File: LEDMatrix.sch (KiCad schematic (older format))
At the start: 75 parts, among them SW1 SW_Push_LED, SW10 SW_Push_LED, SW11 SW_Push_LED, SW12 SW_Push_LED, SW13 SW_Push_LED, SW14 SW_Push_LED, SW15 SW_Push_LED, SW16 SW_Push_LED, SW17 SW_Push_LED, SW18 SW_Push_LED, SW19 SW_Push_LED, SW2 SW_Push_LED, SW20 SW_Push_LED, SW21 SW_Push_LED, SW22 SW_Push_LED, SW23 SW_Push_LED, SW24 SW_Push_LED, SW25 SW_Push_LED, SW26 SW_Push_LED, SW27 SW_Push_LED, SW28 SW_Push_LED, SW29 SW_Push_LED, SW3 SW_Push_LED, SW30 SW_Push_LED, SW31 SW_Push_LED, SW32 SW_Push_LED, SW33 SW_Push_LED, SW34 SW_Push_LED, SW35 SW_Push_LED, SW36 SW_Push_LED, SW37 SW_Push_LED, SW38 SW_Push_LED, SW39 SW_Push_LED, SW4 SW_Push_LED, SW40 SW_Push_LED, SW41 SW_Push_LED, SW42 SW_Push_LED, SW43 SW_Push_LED, SW44 SW_Push_LED, SW45 SW_Push_LED, SW46 SW_Push_LED, SW47 SW_Push_LED, SW48 SW_Push_LED, SW49 SW_Push_LED, SW5 SW_Push_LED, SW50 SW_Push_LED, SW51 SW_Push_LED, SW52 SW_Push_LED, SW53 SW_Push_LED, SW54 SW_Push_LED, SW55 SW_Push_LED, SW56 SW_Push_LED, SW57 SW_Push_LED, SW58 SW_Push_LED, SW59 SW_Push_LED, SW6 SW_Push_LED, SW60 SW_Push_LED, SW61 SW_Push_LED, SW62 SW_Push_LED, SW63 SW_Push_LED, SW64 SW_Push_LED, SW7 SW_Push_LED, SW8 SW_Push_LED, SW9 SW_Push_LED

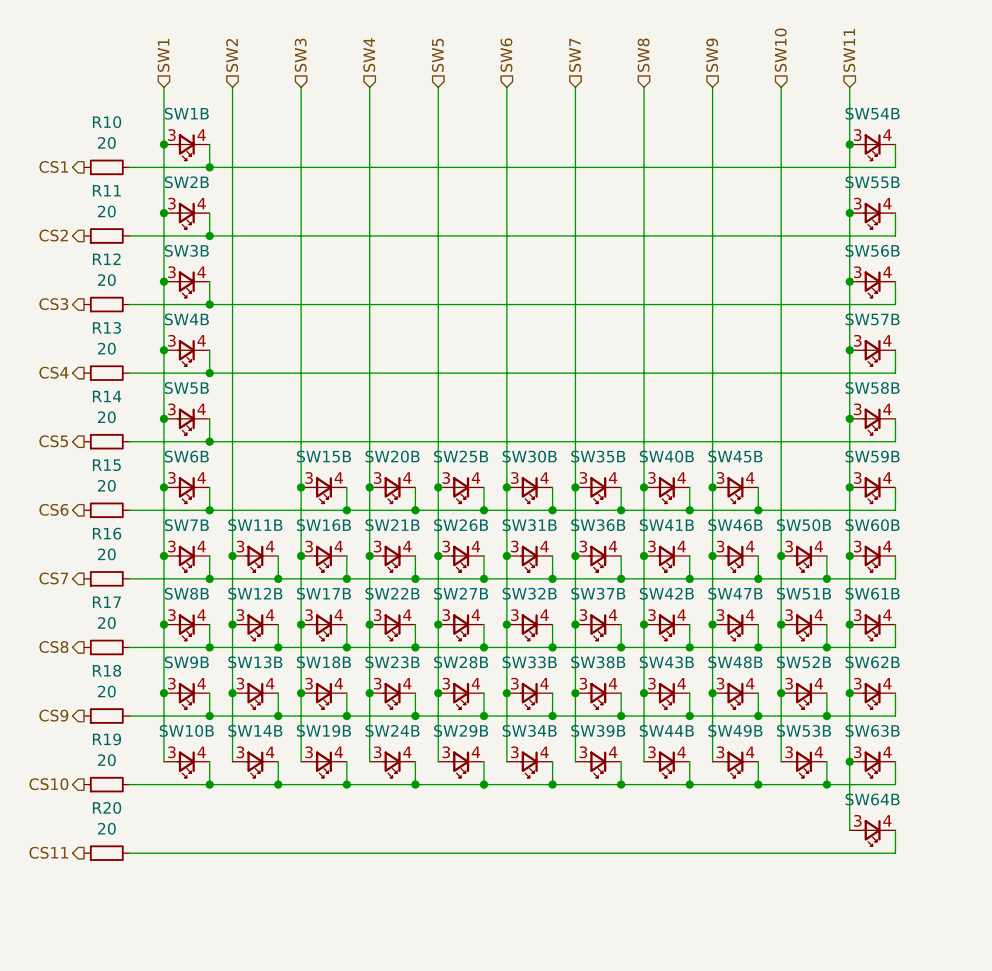
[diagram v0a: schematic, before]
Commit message: Add ATmega32u4 to board
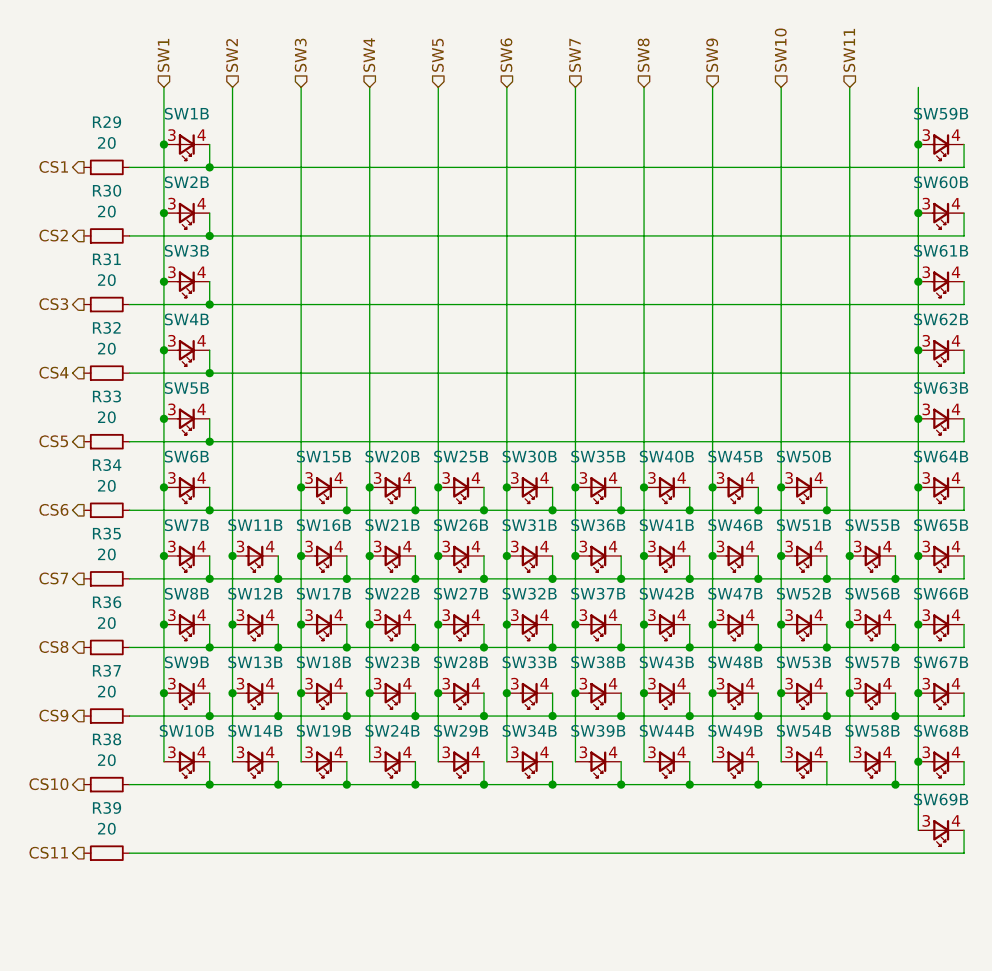
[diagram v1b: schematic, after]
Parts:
- added SW50, SW55, SW56, SW57, SW58: SW_Push_LED, Collins-FMS-3000:SW_PUSH_6mm, symbol Collins-FMS-3000:SW_Push_LED
- R29: renamed from R10; footprint (none) -> Resistor_SMD:R_0402_1005Metric
- R30: renamed from R11; footprint (none) -> Resistor_SMD:R_0402_1005Metric
- R31: renamed from R12; footprint (none) -> Resistor_SMD:R_0402_1005Metric
- R32: renamed from R13; footprint (none) -> Resistor_SMD:R_0402_1005Metric
- R33: renamed from R14; footprint (none) -> Resistor_SMD:R_0402_1005Metric
- R34: renamed from R15; footprint (none) -> Resistor_SMD:R_0402_1005Metric
- R35: renamed from R16; footprint (none) -> Resistor_SMD:R_0402_1005Metric
- R36: renamed from R17; footprint (none) -> Resistor_SMD:R_0402_1005Metric
- R37: renamed from R18; footprint (none) -> Resistor_SMD:R_0402_1005Metric
- R38: renamed from R19; footprint (none) -> Resistor_SMD:R_0402_1005Metric
- R39: renamed from R20; footprint (none) -> Resistor_SMD:R_0402_1005Metric
- SW1, SW10, SW11, SW12, SW13, SW14, SW15, SW16, SW17, SW18, SW19, SW2, SW20, SW21, SW22, SW23, SW24, SW25, SW26, SW27, SW28, SW29, SW3, SW30, SW31, SW32, SW33, SW34, SW35, SW36, SW37, SW38, SW39, SW4, SW40, SW41, SW42, SW43, SW44, SW45, SW46, SW47, SW48, SW49, SW5, SW6, SW7, SW8, SW9: footprint (none) -> Collins-FMS-3000:SW_PUSH_6mm
- SW51: renamed from SW50; footprint (none) -> Collins-FMS-3000:SW_PUSH_6mm
- SW52: renamed from SW51; footprint (none) -> Collins-FMS-3000:SW_PUSH_6mm
- SW53: renamed from SW52; footprint (none) -> Collins-FMS-3000:SW_PUSH_6mm
- SW54: renamed from SW53; footprint (none) -> Collins-FMS-3000:SW_PUSH_6mm
- SW59: renamed from SW54; footprint (none) -> Collins-FMS-3000:SW_PUSH_6mm
- SW60: renamed from SW55; footprint (none) -> Collins-FMS-3000:SW_PUSH_6mm
- SW61: renamed from SW56; footprint (none) -> Collins-FMS-3000:SW_PUSH_6mm
- SW62: renamed from SW57; footprint (none) -> Collins-FMS-3000:SW_PUSH_6mm
- SW63: renamed from SW58; footprint (none) -> Collins-FMS-3000:SW_PUSH_6mm
- SW64: renamed from SW59; footprint (none) -> Collins-FMS-3000:SW_PUSH_6mm
- SW65: renamed from SW60; footprint (none) -> Collins-FMS-3000:SW_PUSH_6mm
- SW66: renamed from SW61; footprint (none) -> Collins-FMS-3000:SW_PUSH_6mm
- SW67: renamed from SW62; footprint (none) -> Collins-FMS-3000:SW_PUSH_6mm
- SW68: renamed from SW63; footprint (none) -> Collins-FMS-3000:SW_PUSH_6mm
- SW69: renamed from SW64; footprint (none) -> Collins-FMS-3000:SW_PUSH_6mm
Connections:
- net SW10: now also SW50.3
- net SW11: now also SW55.3, SW56.3, SW57.3, SW58.3; no longer SW59.3, SW60.3, SW61.3, SW62.3, SW63.3, SW64.3, SW65.3, SW66.3, SW67.3, SW68.3, SW69.3
- net at R34.2, SW15.4, SW20.4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: now also SW50.4
- net at R35.2, SW11.4, SW16.4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: now also SW55.4
- net at R36.2, SW12.4, SW17.4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: now also SW56.4
- net at R37.2, SW13.4, SW18.4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: now also SW57.4
- net at R38.2, SW10.4, SW14.4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: now also SW58.4
- new net: SW59.3, SW60.3, SW61.3, SW62.3, SW63.3, SW64.3, SW65.3, SW66.3, SW67.3, SW68.3, SW69.3
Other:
- moved on the sheet: SW59B, SW60B, SW61B, SW62B, SW63B, SW64B, SW65B, SW66B, SW67B, SW68B, SW69B

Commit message: Redo the LED matrix
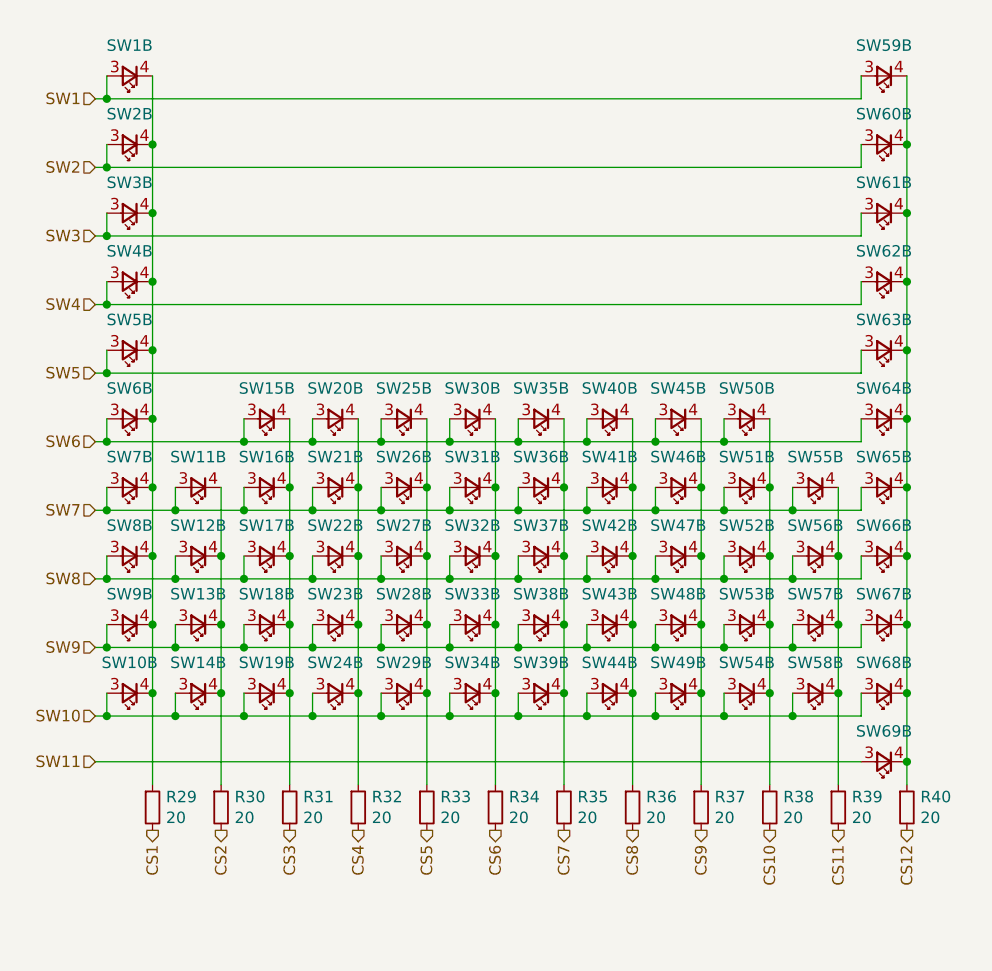
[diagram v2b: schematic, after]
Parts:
- added R40: 20, symbol Device:R_Small
- R29, R30, R31, R32, R33, R34, R35, R36, R37, R38, R39: footprint Resistor_SMD:R_0402_1005Metric -> (none)
- SW1, SW10, SW11, SW12, SW13, SW14, SW15, SW16, SW17, SW18, SW19, SW2, SW20, SW21, SW22, SW23, SW24, SW25, SW26, SW27, SW28, SW29, SW3, SW30, SW31, SW32, SW33, SW34, SW35, SW36, SW37, SW38, SW39, SW4, SW40, SW41, SW42, SW43, SW44, SW45, SW46, SW47, SW48, SW49, SW5, SW50, SW51, SW52, SW53, SW54, SW55, SW56, SW57, SW58, SW59, SW6, SW60, SW61, SW62, SW63, SW64, SW65, SW66, SW67, SW68, SW69, SW7, SW8, SW9: footprint Collins-FMS-3000:SW_PUSH_6mm -> (none)
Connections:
- net CS1: now also R29.2; no longer R29.1
- net CS10: now also R38.2; no longer R38.1
- net CS11: now also R39.2; no longer R39.1
- net CS2: now also R30.2; no longer R30.1
- net CS3: now also R31.2; no longer R31.1
- net CS4: now also R32.2; no longer R32.1
- net CS5: now also R33.2; no longer R33.1
- net CS6: now also R34.2; no longer R34.1
- net CS7: now also R35.2; no longer R35.1
- net CS8: now also R36.2; no longer R36.1
- net CS9: now also R37.2; no longer R37.1
- net SW1: now also SW59.3; no longer SW10.3, SW2.3, SW3.3, SW4.3, SW5.3, SW6.3, SW7.3, SW8.3, SW9.3
- net SW10: now also SW10.3, SW14.3, SW19.3, SW24.3, SW29.3, SW34.3, SW39.3, SW44.3, SW49.3, SW58.3, SW68.3; no longer SW50.3, SW51.3, SW52.3, SW53.3
- net SW11: now also SW69.3; no longer SW55.3, SW56.3, SW57.3, SW58.3
- net SW2: now also SW2.3, SW60.3; no longer SW11.3, SW12.3, SW13.3, SW14.3
- net SW3: now also SW3.3, SW61.3; no longer SW15.3, SW16.3, SW17.3, SW18.3, SW19.3
- net SW4: now also SW4.3, SW62.3; no longer SW20.3, SW21.3, SW22.3, SW23.3, SW24.3
- net SW5: now also SW5.3, SW63.3; no longer SW25.3, SW26.3, SW27.3, SW28.3, SW29.3
- net SW6: now also SW15.3, SW20.3, SW25.3, SW35.3, SW40.3, SW45.3, SW50.3, SW6.3, SW64.3; no longer SW31.3, SW32.3, SW33.3, SW34.3
- net SW7: now also SW11.3, SW16.3, SW21.3, SW26.3, SW31.3, SW41.3, SW46.3, SW51.3, SW55.3, SW65.3, SW7.3; no longer SW35.3, SW37.3, SW38.3, SW39.3
- net SW8: now also SW12.3, SW17.3, SW22.3, SW27.3, SW32.3, SW37.3, SW47.3, SW52.3, SW56.3, SW66.3, SW8.3; no longer SW40.3, SW41.3, SW43.3, SW44.3
- net SW9: now also SW13.3, SW18.3, SW23.3, SW28.3, SW33.3, SW38.3, SW43.3, SW53.3, SW57.3, SW67.3, SW9.3; no longer SW45.3, SW46.3, SW47.3, SW49.3
- net at SW69.4: now also SW59.4, SW60.4, SW61.4, SW62.4, SW63.4, SW64.4, SW65.4, SW66.4, SW67.4, SW68.4, R40.1; no longer R39.2
- new net: R29.1, SW1.4, SW10.4, SW2.4, SW3.4, SW4.4, SW5.4, SW6.4, SW7.4, SW8.4, SW9.4
- new net: R30.1, SW11.4, SW12.4, SW13.4, SW14.4
- new net: R31.1, SW15.4, SW16.4, SW17.4, SW18.4, SW19.4
- new net: R32.1, SW20.4, SW21.4, SW22.4, SW23.4, SW24.4
- new net: R33.1, SW25.4, SW26.4, SW27.4, SW28.4, SW29.4
- new net: R34.1, SW30.4, SW31.4, SW32.4, SW33.4, SW34.4
- new net: R35.1, SW35.4, SW36.4, SW37.4, SW38.4, SW39.4
- new net: R36.1, SW40.4, SW41.4, SW42.4, SW43.4, SW44.4
- new net: R37.1, SW45.4, SW46.4, SW47.4, SW48.4, SW49.4
- new net: R38.1, SW50.4, SW51.4, SW52.4, SW53.4, SW54.4
- new net: R39.1, SW55.4, SW56.4, SW57.4, SW58.4
- new net CS12: R40.2

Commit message: Lots of PCB layout
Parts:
- R29, R30, R31, R32, R33, R34, R35, R36, R37, R38, R39, R40: footprint (none) -> Resistor_SMD:R_0402_1005Metric
- SW1, SW10, SW11, SW12, SW13, SW14, SW15, SW16, SW17, SW18, SW19, SW2, SW20, SW21, SW22, SW23, SW24, SW25, SW26, SW27, SW28, SW29, SW3, SW30, SW31, SW32, SW33, SW34, SW35, SW36, SW37, SW38, SW39, SW4, SW40, SW41, SW42, SW43, SW44, SW45, SW46, SW47, SW48, SW49, SW5, SW50, SW51, SW52, SW53, SW54, SW55, SW56, SW57, SW58, SW59, SW6, SW60, SW61, SW62, SW63, SW64, SW65, SW66, SW67, SW68, SW69, SW7, SW8, SW9: footprint (none) -> Collins-FMS-3000:SW_PUSH_6mm

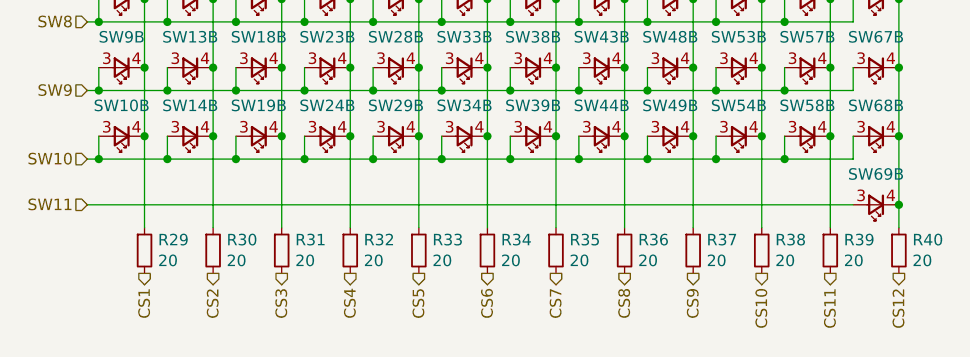
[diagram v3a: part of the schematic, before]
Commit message: New LED chip, tons of routing on the board
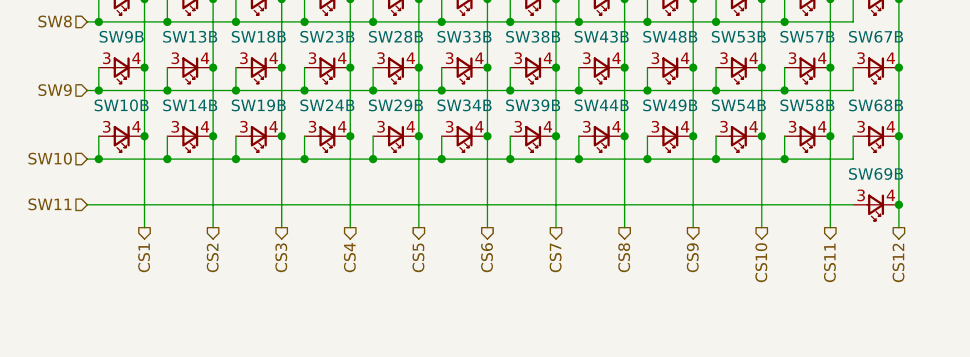
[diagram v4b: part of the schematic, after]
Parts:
- removed R29, R30, R31, R32, R33, R34, R35, R36, R37, R38, R39, R40: 20, Resistor_SMD:R_0402_1005Metric, symbol Device:R_Small
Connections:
- net CS1: now also SW1.4, SW10.4, SW2.4, SW3.4, SW4.4, SW5.4, SW6.4, SW7.4, SW8.4, SW9.4
- net CS10: now also SW50.4, SW51.4, SW52.4, SW53.4, SW54.4
- net CS11: now also SW55.4, SW56.4, SW57.4, SW58.4
- net CS12: now also SW59.4, SW60.4, SW61.4, SW62.4, SW63.4, SW64.4, SW65.4, SW66.4, SW67.4, SW68.4, SW69.4
- net CS2: now also SW11.4, SW12.4, SW13.4, SW14.4
- net CS3: now also SW15.4, SW16.4, SW17.4, SW18.4, SW19.4
- net CS4: now also SW20.4, SW21.4, SW22.4, SW23.4, SW24.4
- net CS5: now also SW25.4, SW26.4, SW27.4, SW28.4, SW29.4
- net CS6: now also SW30.4, SW31.4, SW32.4, SW33.4, SW34.4
- net CS7: now also SW35.4, SW36.4, SW37.4, SW38.4, SW39.4
- net CS8: now also SW40.4, SW41.4, SW42.4, SW43.4, SW44.4
- net CS9: now also SW45.4, SW46.4, SW47.4, SW48.4, SW49.4
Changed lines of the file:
@@
 Wire Wire Line
 	4250 3750 900  3750
-$Comp
-L Device:R_Small R29
-U 1 1 61B42B61
-P 1150 3950
-F 0 "R29" H 1209 3996 50  0000 L CNN
-F 1 "20" H 1209 3905 50  0000 L CNN
-F 2 "Resistor_SMD:R_0402_1005Metric" H 1150 3950 50  0001 C CNN
-F 3 "~" H 1150 3950 50  0001 C CNN
-	1    1150 3950
-	1    0    0    -1
-$EndComp
-$Comp
-L Device:R_Small R30
-U 1 1 61B44613
-P 1450 3950
-F 0 "R30" H 1509 3996 50  0000 L CNN
-F 1 "20" H 1509 3905 50  0000 L CNN
-F 2 "Resistor_SMD:R_0402_1005Metric" H 1450 3950 50  0001 C CNN
-F 3 "~" H 1450 3950 50  0001 C CNN
-	1    1450 3950
-	1    0    0    -1
-$EndComp
-$Comp
-L Device:R_Small R31
-U 1 1 61B5AC10
-P 1750 3950
-F 0 "R31" H 1809 3996 50  0000 L CNN
-F 1 "20" H 1809 3905 50  0000 L CNN
-F 2 "Resistor_SMD:R_0402_1005Metric" H 1750 3950 50  0001 C CNN
-F 3 "~" H 1750 3950 50  0001 C CNN
-	1    1750 3950
-	1    0    0    -1
-$EndComp
-$Comp
-L Device:R_Small R32
-U 1 1 61B71123
-P 2050 3950
-F 0 "R32" H 2109 3996 50  0000 L CNN
-F 1 "20" H 2109 3905 50  0000 L CNN
-F 2 "Resistor_SMD:R_0402_1005Metric" H 2050 3950 50  0001 C CNN
-F 3 "~" H 2050 3950 50  0001 C CNN
-	1    2050 3950
-	1    0    0    -1
-$EndComp
-$Comp
-L Device:R_Small R33
-U 1 1 61B876BE
-P 2350 3950
-F 0 "R33" H 2409 3996 50  0000 L CNN
-F 1 "20" H 2409 3905 50  0000 L CNN
-F 2 "Resistor_SMD:R_0402_1005Metric" H 2350 3950 50  0001 C CNN
-F 3 "~" H 2350 3950 50  0001 C CNN
-	1    2350 3950
-	1    0    0    -1
-$EndComp
-$Comp
-L Device:R_Small R34
-U 1 1 61B9DC44
-P 2650 3950
-F 0 "R34" H 2709 3996 50  0000 L CNN
-F 1 "20" H 2709 3905 50  0000 L CNN
-F 2 "Resistor_SMD:R_0402_1005Metric" H 2650 3950 50  0001 C CNN
-F 3 "~" H 2650 3950 50  0001 C CNN
-	1    2650 3950
-	1    0    0    -1
-$EndComp
-$Comp
-L Device:R_Small R35
-U 1 1 61BB4181
-P 2950 3950
-F 0 "R35" H 3009 3996 50  0000 L CNN
-F 1 "20" H 3009 3905 50  0000 L CNN
-F 2 "Resistor_SMD:R_0402_1005Metric" H 2950 3950 50  0001 C CNN
-F 3 "~" H 2950 3950 50  0001 C CNN
-	1    2950 3950
-	1    0    0    -1
-$EndComp
-$Comp
-L Device:R_Small R36
-U 1 1 61BCA95E
-P 3250 3950
-F 0 "R36" H 3309 3996 50  0000 L CNN
-F 1 "20" H 3309 3905 50  0000 L CNN
-F 2 "Resistor_SMD:R_0402_1005Metric" H 3250 3950 50  0001 C CNN
-F 3 "~" H 3250 3950 50  0001 C CNN
-	1    3250 3950
-	1    0    0    -1
-$EndComp
-$Comp
-L Device:R_Small R37
-U 1 1 61BE0EEA
-P 3550 3950
-F 0 "R37" H 3609 3996 50  0000 L CNN
-F 1 "20" H 3609 3905 50  0000 L CNN
-F 2 "Resistor_SMD:R_0402_1005Metric" H 3550 3950 50  0001 C CNN
-F 3 "~" H 3550 3950 50  0001 C CNN
-	1    3550 3950
-	1    0    0    -1
-$EndComp
-$Comp
-L Device:R_Small R38
-U 1 1 61BF7436
-P 3850 3950
-F 0 "R38" H 3909 3996 50  0000 L CNN
-F 1 "20" H 3909 3905 50  0000 L CNN
-F 2 "Resistor_SMD:R_0402_1005Metric" H 3850 3950 50  0001 C CNN
-F 3 "~" H 3850 3950 50  0001 C CNN
-	1    3850 3950
-	1    0    0    -1
-$EndComp
-$Comp
-L Device:R_Small R39
-U 1 1 61C0DB47
-P 4150 3950
-F 0 "R39" H 4209 3996 50  0000 L CNN
-F 1 "20" H 4209 3905 50  0000 L CNN
-F 2 "Resistor_SMD:R_0402_1005Metric" H 4150 3950 50  0001 C CNN
-F 3 "~" H 4150 3950 50  0001 C CNN
-	1    4150 3950
-	1    0    0    -1
-$EndComp
-$Comp
-L Device:R_Small R40
-U 1 1 61C24289
-P 4450 3950
-F 0 "R40" H 4509 3996 50  0000 L CNN
-F 1 "20" H 4509 3905 50  0000 L CNN
-F 2 "Resistor_SMD:R_0402_1005Metric" H 4450 3950 50  0001 C CNN
-F 3 "~" H 4450 3950 50  0001 C CNN
-	1    4450 3950
-	1    0    0    -1
-$EndComp
-Text HLabel 1150 4050 3    50   Output ~ 0
+Text HLabel 1150 3850 3    50   Output ~ 0
 CS1
-Text HLabel 1450 4050 3    50   Output ~ 0
+Text HLabel 1450 3850 3    50   Output ~ 0
 CS2
-Text HLabel 1750 4050 3    50   Output ~ 0
+Text HLabel 1750 3850 3    50   Output ~ 0
 CS3
-Text HLabel 2050 4050 3    50   Output ~ 0
+Text HLabel 2050 3850 3    50   Output ~ 0
 CS4
-Text HLabel 2350 4050 3    50   Output ~ 0
+Text HLabel 2350 3850 3    50   Output ~ 0
 CS5
-Text HLabel 2650 4050 3    50   Output ~ 0
+Text HLabel 2650 3850 3    50   Output ~ 0
 CS6
-Text HLabel 2950 4050 3    50   Output ~ 0
+Text HLabel 2950 3850 3    50   Output ~ 0
 CS7
-Text HLabel 3250 4050 3    50   Output ~ 0
+Text HLabel 3250 3850 3    50   Output ~ 0
 CS8
-Text HLabel 3550 4050 3    50   Output ~ 0
+Text HLabel 3550 3850 3    50   Output ~ 0
 CS9
-Text HLabel 3850 4050 3    50   Output ~ 0
+Text HLabel 3850 3850 3    50   Output ~ 0
 CS10
-Text HLabel 4150 4050 3    50   Output ~ 0
+Text HLabel 4150 3850 3    50   Output ~ 0
 CS11
-Text HLabel 4450 4050 3    50   Output ~ 0
+Text HLabel 4450 3850 3    50   Output ~ 0
 CS12
 Text HLabel 900  850  0    50   Input ~ 0
